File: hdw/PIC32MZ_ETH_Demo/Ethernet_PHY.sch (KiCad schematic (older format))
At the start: 19 parts

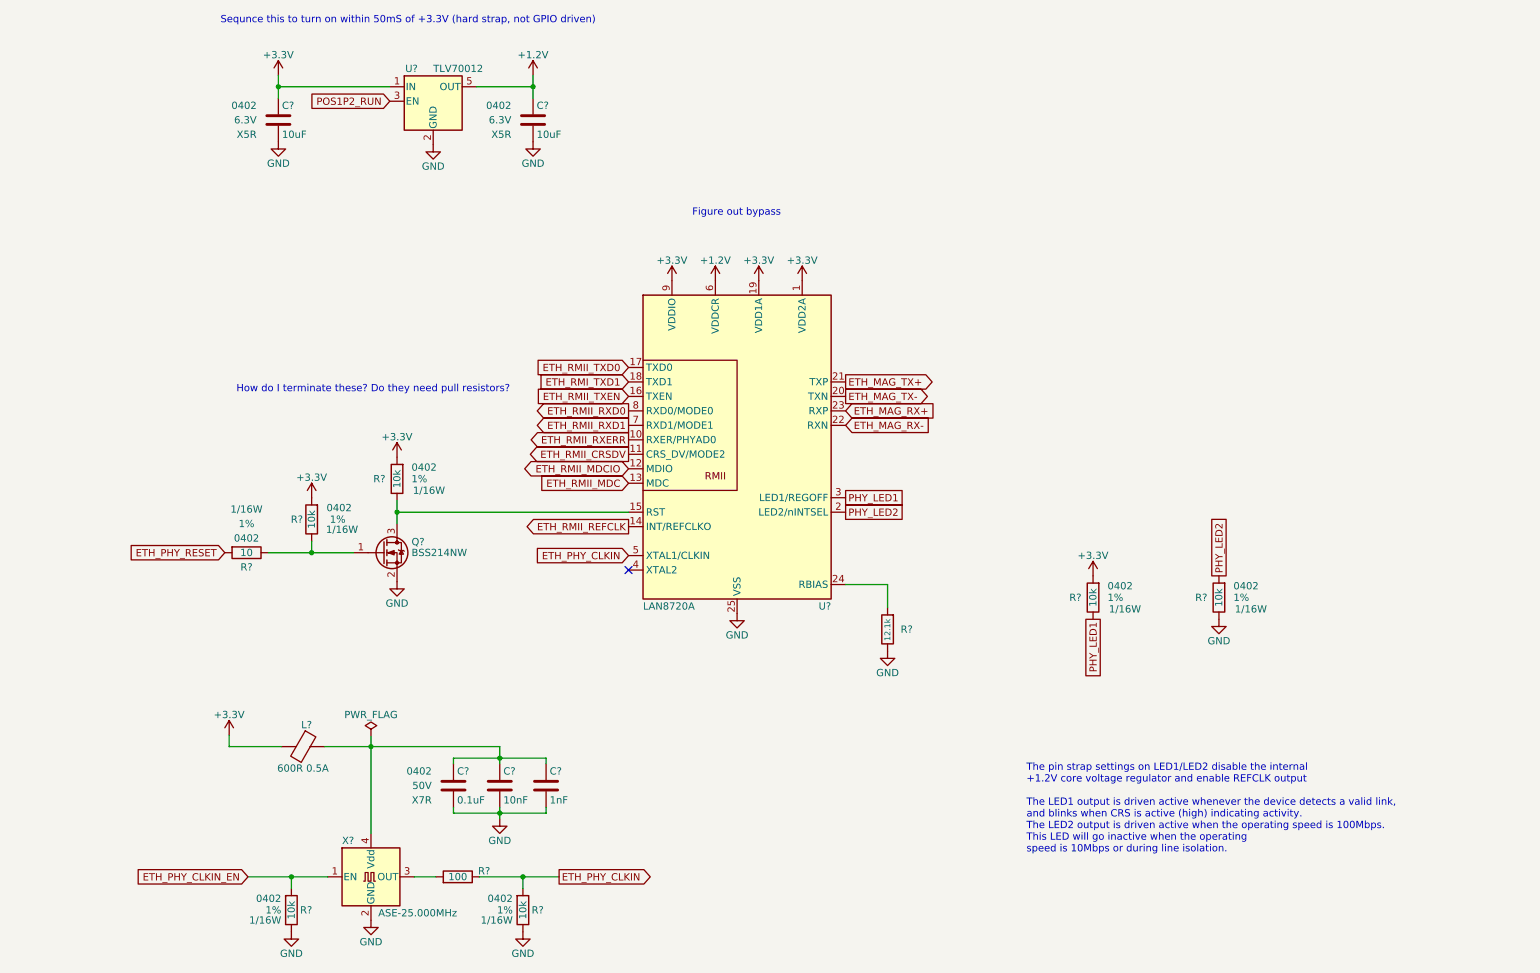
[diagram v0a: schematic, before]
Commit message: More schematic tweaks, followed PHY design guide
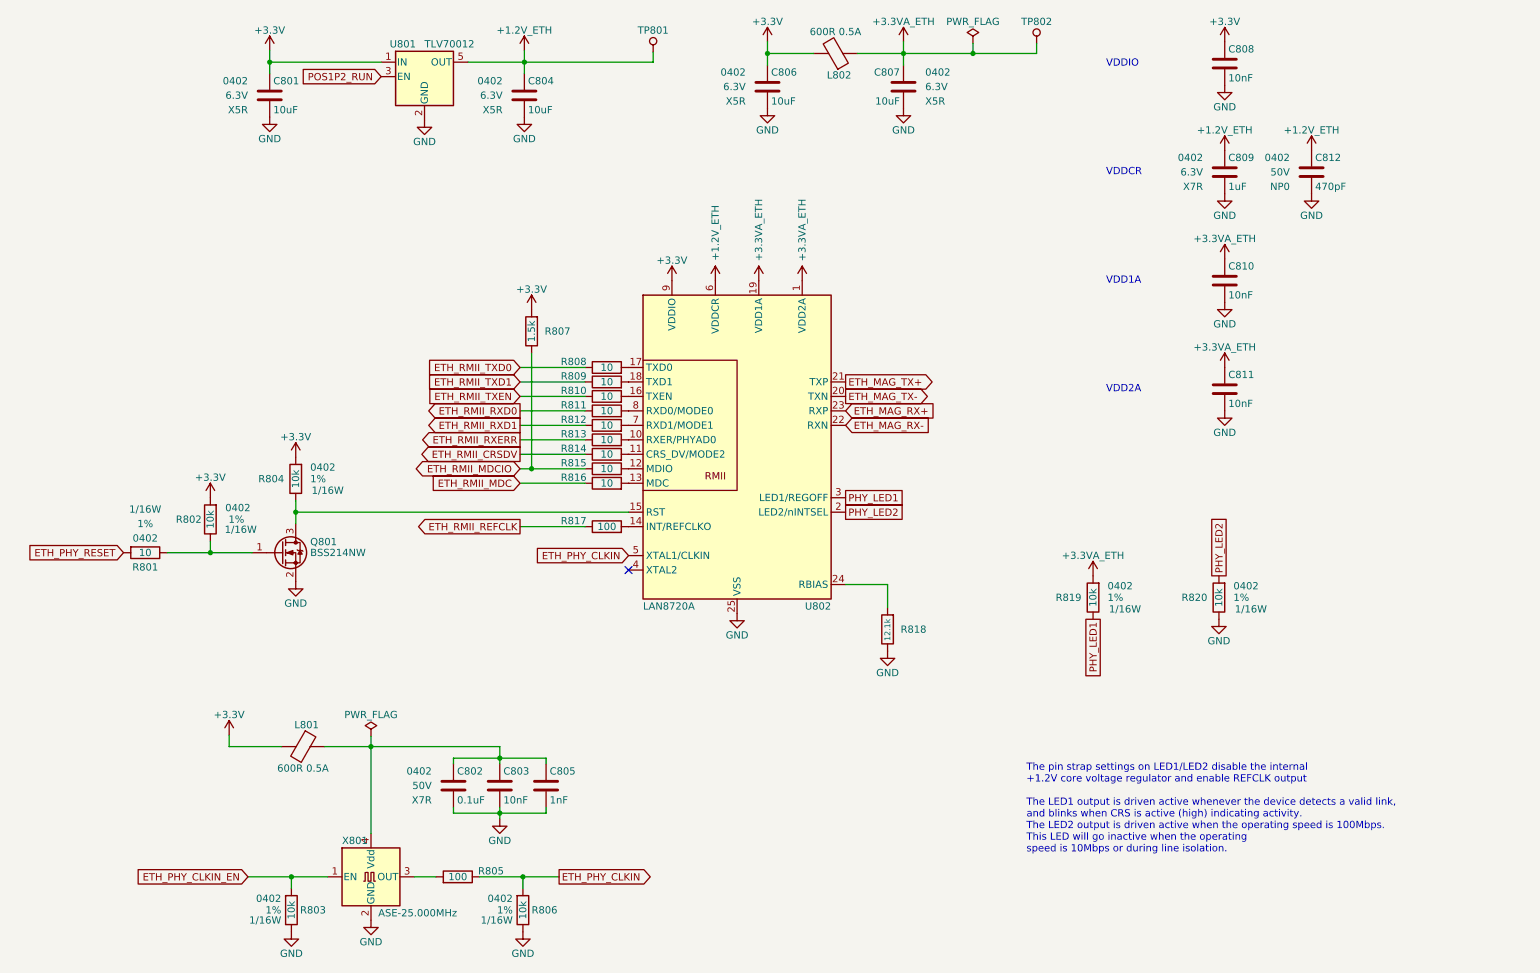
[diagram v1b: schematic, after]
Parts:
- added C806, C807: 10uF, Capacitors_SMD:C_0402, symbol Custom_Library:C_Custom
- added C808, C810, C811: 10nF, Capacitors_SMD:C_0402, symbol Custom_Library:C_Custom
- added C809: 1uF, Capacitors_SMD:C_0402, symbol Custom_Library:C_Custom
- added C812: 470pF, Capacitors_SMD:C_0402, symbol Custom_Library:C_Custom
- added L802: 600R 0.5A, Inductors_SMD:L_0603, symbol Device:Ferrite_Bead
- added R807: 1.5k, symbol Custom_Library:R_Custom
- added R808, R809, R810, R811, R812, R813, R814, R815, R816: 10, Resistors_SMD:R_0402, symbol Custom_Library:R_Custom
- added R817: 100, Resistors_SMD:R_0402, symbol Custom_Library:R_Custom
- added TP801, TP802: TP_Pad, Custom Footprints Library:Test_Point, symbol Custom_Library:TP_Pad
- gave numbers to parts that had none: 19
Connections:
- net +3V3: now also C806.1, C808.1, L802.2, R807.1; no longer R819.1, U802.1 (VDD2A), U802.19 (VDD1A)
- net ETH_RMII_CRSDV: now also R814.2; no longer U802.11 (CRS_DV/MODE2)
- net ETH_RMII_MDC: now also R816.2; no longer U802.13 (MDC)
- net ETH_RMII_MDCIO: now also R807.2, R815.2; no longer U802.12 (MDIO)
- net ETH_RMII_REFCLK: now also R817.2; no longer U802.14 (INT/REFCLKO)
- net ETH_RMII_RXD0: now also R811.2; no longer U802.8 (RXD0/MODE0)
- net ETH_RMII_RXD1: now also R812.2; no longer U802.7 (RXD1/MODE1)
- net ETH_RMII_RXERR: now also R813.2; no longer U802.10 (RXER/PHYAD0)
- net ETH_RMII_TXD0: now also R808.2; no longer U802.17 (TXD0)
- net ETH_RMII_TXEN: now also R810.2; no longer U802.16 (TXEN)
- net GND: now also C806.2, C807.2, C808.2, C809.2, C810.2, C811.2, C812.2
- net +1.2V renamed +1.2V_ETH
- net +1.2V_ETH: now also C809.1, C812.1, TP801.1 (TP)
- net ETH_RMI_TXD1: no longer names the net of U802.18 (TXD1)
- net ETH_RMI_TXD1: now also R809.1
- new net: R813.1, U802.10 (RXER/PHYAD0)
- new net: R814.1, U802.11 (CRS_DV/MODE2)
- new net: R815.1, U802.12 (MDIO)
- new net: R816.1, U802.13 (MDC)
- new net: R817.1, U802.14 (INT/REFCLKO)
- new net: R810.1, U802.16 (TXEN)
- new net: R808.1, U802.17 (TXD0)
- new net: R812.1, U802.7 (RXD1/MODE1)
- new net: R811.1, U802.8 (RXD0/MODE0)
- new net +3.3VA_ETH: C807.1, C810.1, C811.1, L802.1, R819.1, TP802.1 (TP), U802.1 (VDD2A), U802.19 (VDD1A)
- new net ETH_RMII_TXD1: R809.2
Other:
- note added: "VDD1A"
- note added: "VDD2A"
- note added: "VDDCR"
- note added: "VDDIO"
- note removed: "Figure out bypass"
- note removed: "How do I terminate these? Do they need pull resistors?"
- note removed: "Sequnce this to turn on within 50mS of +3.3V (hard strap, not GPIO driven)"
- moved on the sheet: C801, C804, Q801, R801, R802, R804, U801

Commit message: Populated digi-key pn's
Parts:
- C801, C804, C806, C807: Digi-Key PN (none) -> 490-13211-1-ND
- C802: Digi-Key PN (none) -> 490-10701-1-ND
- C803, C808, C810, C811: Digi-Key PN (none) -> 490-13295-1-ND
- C805: Digi-Key PN (none) -> 399-1032-1-ND
- C809: Digi-Key PN (none) -> 490-9665-1-ND
- C812: Digi-Key PN (none) -> 399-1025-1-ND
- L801, L802: footprint Inductors_SMD:L_0603 -> Inductors_SMD:L_0402; Digi-Key PN (none) -> 490-5441-1-ND
- R801, R808, R809, R810, R811, R812, R813, R814, R815, R816: Digi-Key PN (none) -> 541-3964-1-ND
- R802, R803, R804, R806, R819, R820: Digi-Key PN (none) -> RMCF0402FT10K0CT-ND
- R805, R817: Digi-Key PN (none) -> 541-100LCT-ND
- R807: footprint (none) -> Resistors_SMD:R_0402; Digi-Key PN PN -> 541-1.50KLCT-ND
- R818: footprint (none) -> Resistors_SMD:R_0402; Digi-Key PN PN -> 541-CRCW040212K1FKTDCT-ND
- U801: Digi-Key PN (none) -> 296-27438-1-ND
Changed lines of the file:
@@
 F 0 "R818" H 6550 5020 50  0000 L CNN
 F 1 "12.1k" V 6460 4940 40  0000 L CNN
-F 2 "" H 6460 5020 50  0001 C CNN
+F 2 "Resistors_SMD:R_0402" H 6460 5020 50  0001 C CNN
 F 3 "" H 6460 5020 50  0001 C CNN
 F 4 "0402" V 6560 5020 50  0001 C CNN "display_footprint"
 F 5 "1%" V 6660 5020 50  0001 C CNN "Tolerance"
 F 6 "1/16W" V 6760 5020 50  0001 C CNN "Wattage"
-F 7 "PN" H 6760 5420 60  0001 C CNN "Digi-Key PN"
+F 7 "541-CRCW040212K1FKTDCT-ND" H 6760 5420 60  0001 C CNN "Digi-Key PN"
 	1    6460 5020
 	1    0    0    -1
@@
 F 2 "Package_TO_SOT_SMD:SOT-353_SC-70-5" H 3260 1500 50  0001 C CIN
 F 3 "http://www.ti.com/lit/ds/symlink/tlv700.pdf" H 3260 1250 50  0001 C CNN
+F 4 "296-27438-1-ND" H 3260 1200 50  0001 C CNN "Digi-Key PN"
 	1    3260 1200
 	1    0    0    -1
@@
 F 5 "6.3V" H 2040 1330 50  0000 R CNN "Voltage"
 F 6 "X5R" H 2040 1230 50  0000 R CNN "Dielectric"
-F 7 "" H 2190 1330 50  0001 C CNN "Digi-Key PN"
+F 7 "490-13211-1-ND" H 2190 1330 50  0001 C CNN "Digi-Key PN"
 	1    2190 1330
 	1    0    0    -1
@@
 F 5 "6.3V" H 3800 1330 50  0000 R CNN "Voltage"
 F 6 "X5R" H 3800 1230 50  0000 R CNN "Dielectric"
-F 7 "" H 3950 1330 50  0001 C CNN "Digi-Key PN"
+F 7 "490-13211-1-ND" H 3950 1330 50  0001 C CNN "Digi-Key PN"
 	1    3950 1330
 	1    0    0    -1
@@
 F 5 "1%" H 4010 6960 50  0000 L CNN "Tolerance"
 F 6 "1/16W" H 4010 6890 50  0000 L CNN "Wattage"
-F 7 "" H 3940 6960 50  0001 C CNN "Digi-Key PN"
+F 7 "RMCF0402FT10K0CT-ND" H 3940 6960 50  0001 C CNN "Digi-Key PN"
 	1    3940 6960
 	-1   0    0    -1
@@
 F 5 "1%" V 3690 6730 50  0001 C CNN "Tolerance"
 F 6 "1/16W" V 3790 6730 50  0001 C CNN "Wattage"
-F 7 "" H 3790 7130 60  0001 C CNN "Digi-Key PN"
+F 7 "541-100LCT-ND" H 3790 7130 60  0001 C CNN "Digi-Key PN"
 	1    3490 6730
 	0    -1   1    0
@@
 F 5 "1%" H 2410 6960 50  0000 L CNN "Tolerance"
 F 6 "1/16W" H 2410 6890 50  0000 L CNN "Wattage"
-F 7 "" H 2340 6960 50  0001 C CNN "Digi-Key PN"
+F 7 "RMCF0402FT10K0CT-ND" H 2340 6960 50  0001 C CNN "Digi-Key PN"
 	1    2340 6960
 	-1   0    0    -1
@@
 F 5 "50V" H 3310 6100 50  0000 R CNN "Voltage"
 F 6 "X7R" H 3310 6000 50  0000 R CNN "Dielectric"
-F 7 "" H -450 -780 50  0001 C CNN "Digi-Key PN"
+F 7 "490-10701-1-ND" H -450 -780 50  0001 C CNN "Digi-Key PN"
 	1    3460 6100
 	1    0    0    -1
@@
 F 5 "50V" H 3950 6100 50  0001 R CNN "Voltage"
 F 6 "X7R" H 3950 6000 50  0001 R CNN "Dielectric"
-F 7 "" H -450 -780 50  0001 C CNN "Digi-Key PN"
+F 7 "399-1032-1-ND" H -450 -780 50  0001 C CNN "Digi-Key PN"
 	1    4100 6100
 	1    0    0    -1
@@
 F 5 "50V" H 3630 6100 50  0001 R CNN "Voltage"
 F 6 "X7R" H 3630 6000 50  0001 R CNN "Dielectric"
-F 7 "" H -450 -780 50  0001 C CNN "Digi-Key PN"
+F 7 "490-13295-1-ND" H -450 -780 50  0001 C CNN "Digi-Key PN"
 	1    3780 6100
 	1    0    0    -1
@@
 F 0 "L801" V 2270 5855 50  0000 C CNN
 F 1 "600R 0.5A" V 2570 5830 50  0000 C CNN
-F 2 "Inductors_SMD:L_0603" V 2350 5830 50  0001 C CNN
+F 2 "Inductors_SMD:L_0402" V 2350 5830 50  0001 C CNN
 F 3 "~" H 2420 5830 50  0001 C CNN
-F 4 "" H -5770 2740 50  0001 C CNN "Digi-Key PN"
+F 4 "490-5441-1-ND" H -5770 2740 50  0001 C CNN "Digi-Key PN"
 	1    2420 5830
 	0    1    1    0
@@
 F 5 "1%" H 2470 3980 50  0000 L CNN "Tolerance"
 F 6 "1/16W" H 2480 3900 50  0000 L CNN "Wattage"
-F 7 "" H 2670 4380 60  0001 C CNN "Digi-Key PN"
+F 7 "RMCF0402FT10K0CT-ND" H 2670 4380 60  0001 C CNN "Digi-Key PN"
 	1    2370 3980
 	1    0    0    -1
@@
 F 5 "1%" V 1530 4490 50  0000 C CNN "Tolerance"
 F 6 "1/16W" V 1630 4490 50  0000 C CNN "Wattage"
-F 7 "" H 1630 4890 60  0001 C CNN "Digi-Key PN"
+F 7 "541-3964-1-ND" H 1630 4890 60  0001 C CNN "Digi-Key PN"
 	1    1330 4490
 	0    -1   -1   0
@@
 F 5 "1%" H 1960 4260 50  0000 C CNN "Tolerance"
 F 6 "1/16W" H 1990 4190 50  0000 C CNN "Wattage"
-F 7 "" H 2080 4660 60  0001 C CNN "Digi-Key PN"
+F 7 "RMCF0402FT10K0CT-ND" H 2080 4660 60  0001 C CNN "Digi-Key PN"
 	1    1780 4260
 	1    0    0    -1
@@
 F 5 "1%" H 7980 4800 50  0000 L CNN "Tolerance"
 F 6 "1/16W" H 7990 4720 50  0000 L CNN "Wattage"
-F 7 "" H 8180 5200 60  0001 C CNN "Digi-Key PN"
+F 7 "RMCF0402FT10K0CT-ND" H 8180 5200 60  0001 C CNN "Digi-Key PN"
 	1    7880 4800
 	1    0    0    -1
@@
 F 5 "1%" H 8850 4800 50  0000 L CNN "Tolerance"
 F 6 "1/16W" H 8860 4720 50  0000 L CNN "Wattage"
-F 7 "" H 9050 5200 60  0001 C CNN "Digi-Key PN"
+F 7 "RMCF0402FT10K0CT-ND" H 9050 5200 60  0001 C CNN "Digi-Key PN"
 	1    8750 4800
 	1    0    0    -1
@@
 F 5 "6.3V" H 8640 1860 50  0000 R CNN "Voltage"
 F 6 "X7R" H 8640 1760 50  0000 R CNN "Dielectric"
+F 7 "490-9665-1-ND" H 8790 1860 50  0001 C CNN "Digi-Key PN"
 	1    8790 1860
 	1    0    0    -1
@@
 F 5 "50V" H 9240 1860 50  0000 R CNN "Voltage"
 F 6 "NP0" H 9240 1760 50  0000 R CNN "Dielectric"
+F 7 "399-1025-1-ND" H 9390 1860 50  0001 C CNN "Digi-Key PN"
 	1    9390 1860
 	1    0    0    -1
@@
 F 0 "L802" V 5950 1065 50  0000 C CNN
 F 1 "600R 0.5A" V 6250 1040 50  0000 C CNN
-F 2 "Inductors_SMD:L_0603" V 6030 1040 50  0001 C CNN
+F 2 "Inductors_SMD:L_0402" V 6030 1040 50  0001 C CNN
 F 3 "~" H 6100 1040 50  0001 C CNN
-F 4 "" H -2090 -2050 50  0001 C CNN "Digi-Key PN"
+F 4 "490-5441-1-ND" H -2090 -2050 50  0001 C CNN "Digi-Key PN"
 	1    6100 1040
 	0    1    -1   0
@@
 F 5 "6.3V" H 5480 1270 50  0000 R CNN "Voltage"
 F 6 "X5R" H 5480 1170 50  0000 R CNN "Dielectric"
-F 7 "" H 5630 1270 50  0001 C CNN "Digi-Key PN"
+F 7 "490-13211-1-ND" H 5630 1270 50  0001 C CNN "Digi-Key PN"
 	1    5630 1270
 	1    0    0    -1
@@
 F 5 "6.3V" H 6420 1270 50  0000 R CNN "Voltage"
 F 6 "X5R" H 6420 1170 50  0000 R CNN "Dielectric"
-F 7 "" H 6570 1270 50  0001 C CNN "Digi-Key PN"
+F 7 "490-13211-1-ND" H 6570 1270 50  0001 C CNN "Digi-Key PN"
 	1    6570 1270
 	-1   0    0    -1
@@
 F 5 "50V" H 8640 1110 50  0001 R CNN "Voltage"
 F 6 "X7R" H 8640 1010 50  0001 R CNN "Dielectric"
-F 7 "" H 4560 -5770 50  0001 C CNN "Digi-Key PN"
+F 7 "490-13295-1-ND" H 4560 -5770 50  0001 C CNN "Digi-Key PN"
 	1    8790 1110
 	1    0    0    -1
@@
 F 5 "50V" H 8640 2610 50  0001 R CNN "Voltage"
 F 6 "X7R" H 8640 2510 50  0001 R CNN "Dielectric"
-F 7 "" H 4560 -4270 50  0001 C CNN "Digi-Key PN"
+F 7 "490-13295-1-ND" H 4560 -4270 50  0001 C CNN "Digi-Key PN"
 	1    8790 2610
 	1    0    0    -1
@@
 F 5 "50V" H 8640 3360 50  0001 R CNN "Voltage"
 F 6 "X7R" H 8640 3260 50  0001 R CNN "Dielectric"
-F 7 "" H 4560 -3520 50  0001 C CNN "Digi-Key PN"
+F 7 "490-13295-1-ND" H 4560 -3520 50  0001 C CNN "Digi-Key PN"
 	1    8790 3360
 	1    0    0    -1
@@
 F 5 "1%" V 4720 4310 50  0001 C CNN "Tolerance"
 F 6 "1/16W" V 4820 4310 50  0001 C CNN "Wattage"
-F 7 "" H 4820 4710 60  0001 C CNN "Digi-Key PN"
+F 7 "541-100LCT-ND" H 4820 4710 60  0001 C CNN "Digi-Key PN"
 	1    4520 4310
 	0    1    1    0
@@
 F 5 "1%" V 4720 4010 50  0001 C CNN "Tolerance"
 F 6 "1/16W" V 4820 4010 50  0001 C CNN "Wattage"
+F 7 "541-3964-1-ND" H 4520 4010 50  0001 C CNN "Digi-Key PN"
 	1    4520 4010
 	0    1    1    0
@@
 F 5 "1%" V 4720 3910 50  0001 C CNN "Tolerance"
 F 6 "1/16W" V 4820 3910 50  0001 C CNN "Wattage"
+F 7 "541-3964-1-ND" H 4520 3910 50  0001 C CNN "Digi-Key PN"
 	1    4520 3910
 	0    1    1    0
@@
 F 5 "1%" V 4720 3810 50  0001 C CNN "Tolerance"
 F 6 "1/16W" V 4820 3810 50  0001 C CNN "Wattage"
+F 7 "541-3964-1-ND" H 4520 3810 50  0001 C CNN "Digi-Key PN"
 	1    4520 3810
 	0    1    1    0
@@
 F 5 "1%" V 4720 3710 50  0001 C CNN "Tolerance"
 F 6 "1/16W" V 4820 3710 50  0001 C CNN "Wattage"
+F 7 "541-3964-1-ND" H 4520 3710 50  0001 C CNN "Digi-Key PN"
 	1    4520 3710
 	0    1    1    0
@@
 F 5 "1%" V 4720 3610 50  0001 C CNN "Tolerance"
 F 6 "1/16W" V 4820 3610 50  0001 C CNN "Wattage"
+F 7 "541-3964-1-ND" H 4520 3610 50  0001 C CNN "Digi-Key PN"
 	1    4520 3610
 	0    1    1    0
@@
 F 5 "1%" V 4720 3510 50  0001 C CNN "Tolerance"
 F 6 "1/16W" V 4820 3510 50  0001 C CNN "Wattage"
+F 7 "541-3964-1-ND" H 4520 3510 50  0001 C CNN "Digi-Key PN"
 	1    4520 3510
 	0    1    1    0
@@
 F 5 "1%" V 4720 3410 50  0001 C CNN "Tolerance"
 F 6 "1/16W" V 4820 3410 50  0001 C CNN "Wattage"
+F 7 "541-3964-1-ND" H 4520 3410 50  0001 C CNN "Digi-Key PN"
 	1    4520 3410
 	0    1    1    0
@@
 F 5 "1%" V 4720 3310 50  0001 C CNN "Tolerance"
 F 6 "1/16W" V 4820 3310 50  0001 C CNN "Wattage"
+F 7 "541-3964-1-ND" H 4520 3310 50  0001 C CNN "Digi-Key PN"
 	1    4520 3310
 	0    1    1    0
@@
 F 5 "1%" V 4720 3210 50  0001 C CNN "Tolerance"
 F 6 "1/16W" V 4820 3210 50  0001 C CNN "Wattage"
+F 7 "541-3964-1-ND" H 4520 3210 50  0001 C CNN "Digi-Key PN"
 	1    4520 3210
 	0    1    1    0
@@
 F 0 "R807" H 4090 2960 50  0000 L CNN
 F 1 "1.5k" V 4000 2960 50  0000 C CNN
-F 2 "" H 4000 2960 50  0001 C CNN
+F 2 "Resistors_SMD:R_0402" H 4000 2960 50  0001 C CNN
 F 3 "" H 4000 2960 50  0001 C CNN
 F 4 "0402" V 4100 2960 50  0001 C CNN "display_footprint"
 F 5 "1%" V 4200 2960 50  0001 C CNN "Tolerance"
 F 6 "1/16W" V 4300 2960 50  0001 C CNN "Wattage"
-F 7 "PN" H 4300 3360 60  0001 C CNN "Digi-Key PN"
+F 7 "541-1.50KLCT-ND" H 4300 3360 60  0001 C CNN "Digi-Key PN"
 	1    4000 2960
 	1    0    0    -1
